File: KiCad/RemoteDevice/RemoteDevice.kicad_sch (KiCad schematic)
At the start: 55 parts, among them J1 Alim, Q1 PJA3411, Q2 PJA3411, SW1 BP, SW2 BP, U1 XC9140, U10 XBEE-3, U2 STM32L041F6Px, U3 MCP6281, U4 ADT7410TRZ, U5 MCP6281, U6 RT606, U7 Microphone, U8 LD2981CU33, U9 Con_4pts

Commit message: routage terminé, proto à envoyer à José
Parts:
- removed J1: Alim, LibKiCad_PjtDeviceManagePV:PinHeader2pts, symbol Connector:Conn_01x02_Male
- added J1, J2: pin, LibKiCad_PjtDeviceManagePV:PinHeader1Pt, symbol LibKiCad_PjtDeviceManagePV:Conn_01x01_Male
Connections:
- net GND: now also J2.1 (Pin_1)
- net piles: now also J1.1 (Pin_1)
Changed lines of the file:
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@@
+    (pin "1")
+  )
+  (symbol (lib_id "LibKiCad_PjtDeviceManagePV:Conn_01x01_Male") (at 19.05 57.15 0) (unit 1)
+    (in_bom yes) (on_board yes)
+    (property "Reference" "J2" (id 0) (at 16.51 57.15 0))
+    (property "Value" "pin" (id 1) (at 21.59 58.42 0))
+    (property "Footprint" "LibKiCad_PjtDeviceManagePV:PinHeader1Pt" (id 2) (at 19.05 57.15 0)
+      (effects (font (size 1.27 1.27)) hide)
+    )
+    (property "Datasheet" "~" (id 3) (at 19.05 57.15 0)
+      (effects (font (size 1.27 1.27)) hide)
+    )
     (pin "1")
   )
@@
     (pin "2")
     (pin "3")
-  )
-  (symbol (lib_id "Connector:Conn_01x02_Male") (at 19.05 54.61 0) (unit 1)
-    (in_bom yes) (on_board yes) (fields_autoplaced)
-    (property "Reference" "J1" (id 0) (at 19.685 49.53 0))
-    (property "Value" "Alim" (id 1) (at 19.685 52.07 0))
-    (property "Footprint" "LibKiCad_PjtDeviceManagePV:PinHeader2pts" (id 2) (at 19.05 54.61 0)
-      (effects (font (size 1.27 1.27)) hide)
-    )
-    (property "Datasheet" "~" (id 3) (at 19.05 54.61 0)
-      (effects (font (size 1.27 1.27)) hide)
-    )
-    (pin "1")
-    (pin "2")
   )
   (symbol (lib_id "power:PWR_FLAG") (at 77.47 49.53 0) (unit 1)
@@
     )
     (property "Datasheet" "" (id 3) (at 148.59 72.39 0)
+      (effects (font (size 1.27 1.27)) hide)
+    )
+    (pin "1")
+  )
+  (symbol (lib_id "LibKiCad_PjtDeviceManagePV:Conn_01x01_Male") (at 19.05 54.61 0) (unit 1)
+    (in_bom yes) (on_board yes)
+    (property "Reference" "J1" (id 0) (at 16.51 54.61 0))
+    (property "Value" "pin" (id 1) (at 21.59 52.07 0))
+    (property "Footprint" "LibKiCad_PjtDeviceManagePV:PinHeader1Pt" (id 2) (at 19.05 54.61 0)
+      (effects (font (size 1.27 1.27)) hide)
+    )
+    (property "Datasheet" "~" (id 3) (at 19.05 54.61 0)
       (effects (font (size 1.27 1.27)) hide)
     )
@@
       (reference "D4") (unit 1) (value "BAT43W-V") (footprint "Diode_SMD:D_SOD-123")
     )
-    (path "/57c017b0-5147-469f-9dad-ed678c57ce92"
-      (reference "J1") (unit 1) (value "Alim") (footprint "LibKiCad_PjtDeviceManagePV:PinHeader2pts")
+    (path "/d3ae2a9d-452c-4e1c-b009-c846d4a4e6df"
+      (reference "J1") (unit 1) (value "pin") (footprint "LibKiCad_PjtDeviceManagePV:PinHeader1Pt")
+    )
+    (path "/3c43b862-699a-4806-8267-7fe24bc43c02"
+      (reference "J2") (unit 1) (value "pin") (footprint "LibKiCad_PjtDeviceManagePV:PinHeader1Pt")
     )
     (path "/a9057e0b-279b-43fc-996f-a2889cba57e3"

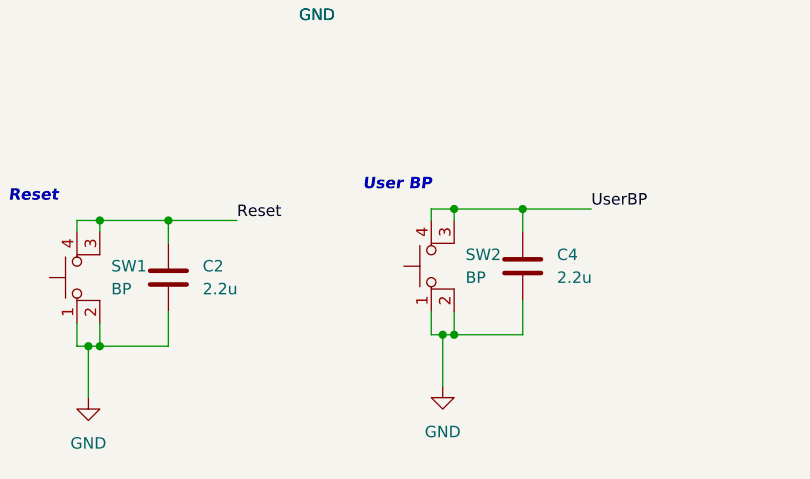
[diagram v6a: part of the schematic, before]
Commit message: Routage revu (tailles condensateur sur switchs). Version envoyée à José le 20 06 2022
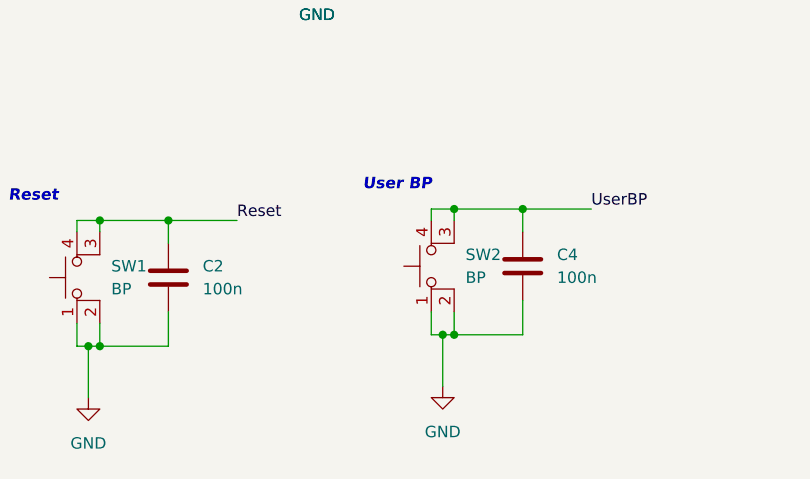
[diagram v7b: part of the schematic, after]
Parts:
- C2, C4: value 2.2u -> 100n; footprint Capacitor_SMD:C_1812_4532Metric -> Capacitor_SMD:C_1206_3216Metric
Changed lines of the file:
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@@
       (effects (font (size 1.27 1.27)) (justify left))
     )
-    (property "Value" "2.2u" (id 1) (at 77.47 172.7199 0)
-      (effects (font (size 1.27 1.27)) (justify left))
-    )
-    (property "Footprint" "Capacitor_SMD:C_1812_4532Metric" (id 2) (at 74.6252 175.26 0)
+    (property "Value" "100n" (id 1) (at 77.47 172.7199 0)
+      (effects (font (size 1.27 1.27)) (justify left))
+    )
+    (property "Footprint" "Capacitor_SMD:C_1206_3216Metric" (id 2) (at 74.6252 175.26 0)
       (effects (font (size 1.27 1.27)) hide)
     )
@@
       (effects (font (size 1.27 1.27)) (justify left))
     )
-    (property "Value" "2.2u" (id 1) (at 38.1 173.9899 0)
-      (effects (font (size 1.27 1.27)) (justify left))
-    )
-    (property "Footprint" "Capacitor_SMD:C_1812_4532Metric" (id 2) (at 35.2552 176.53 0)
+    (property "Value" "100n" (id 1) (at 38.1 173.9899 0)
+      (effects (font (size 1.27 1.27)) (justify left))
+    )
+    (property "Footprint" "Capacitor_SMD:C_1206_3216Metric" (id 2) (at 35.2552 176.53 0)
       (effects (font (size 1.27 1.27)) hide)
     )
@@
     )
     (path "/7be684da-a8e2-4205-844b-38b6f10d367e"
-      (reference "C2") (unit 1) (value "2.2u") (footprint "Capacitor_SMD:C_1812_4532Metric")
+      (reference "C2") (unit 1) (value "100n") (footprint "Capacitor_SMD:C_1206_3216Metric")
     )
     (path "/8cdfe25e-4b7d-4013-8124-b3c01f18588e"
@@
     )
     (path "/10230143-c151-439b-9c31-460a1c05ff46"
-      (reference "C4") (unit 1) (value "2.2u") (footprint "Capacitor_SMD:C_1812_4532Metric")
+      (reference "C4") (unit 1) (value "100n") (footprint "Capacitor_SMD:C_1206_3216Metric")
     )
     (path "/bf597f3e-5fb8-4897-ac09-bc00b0cf2f92"

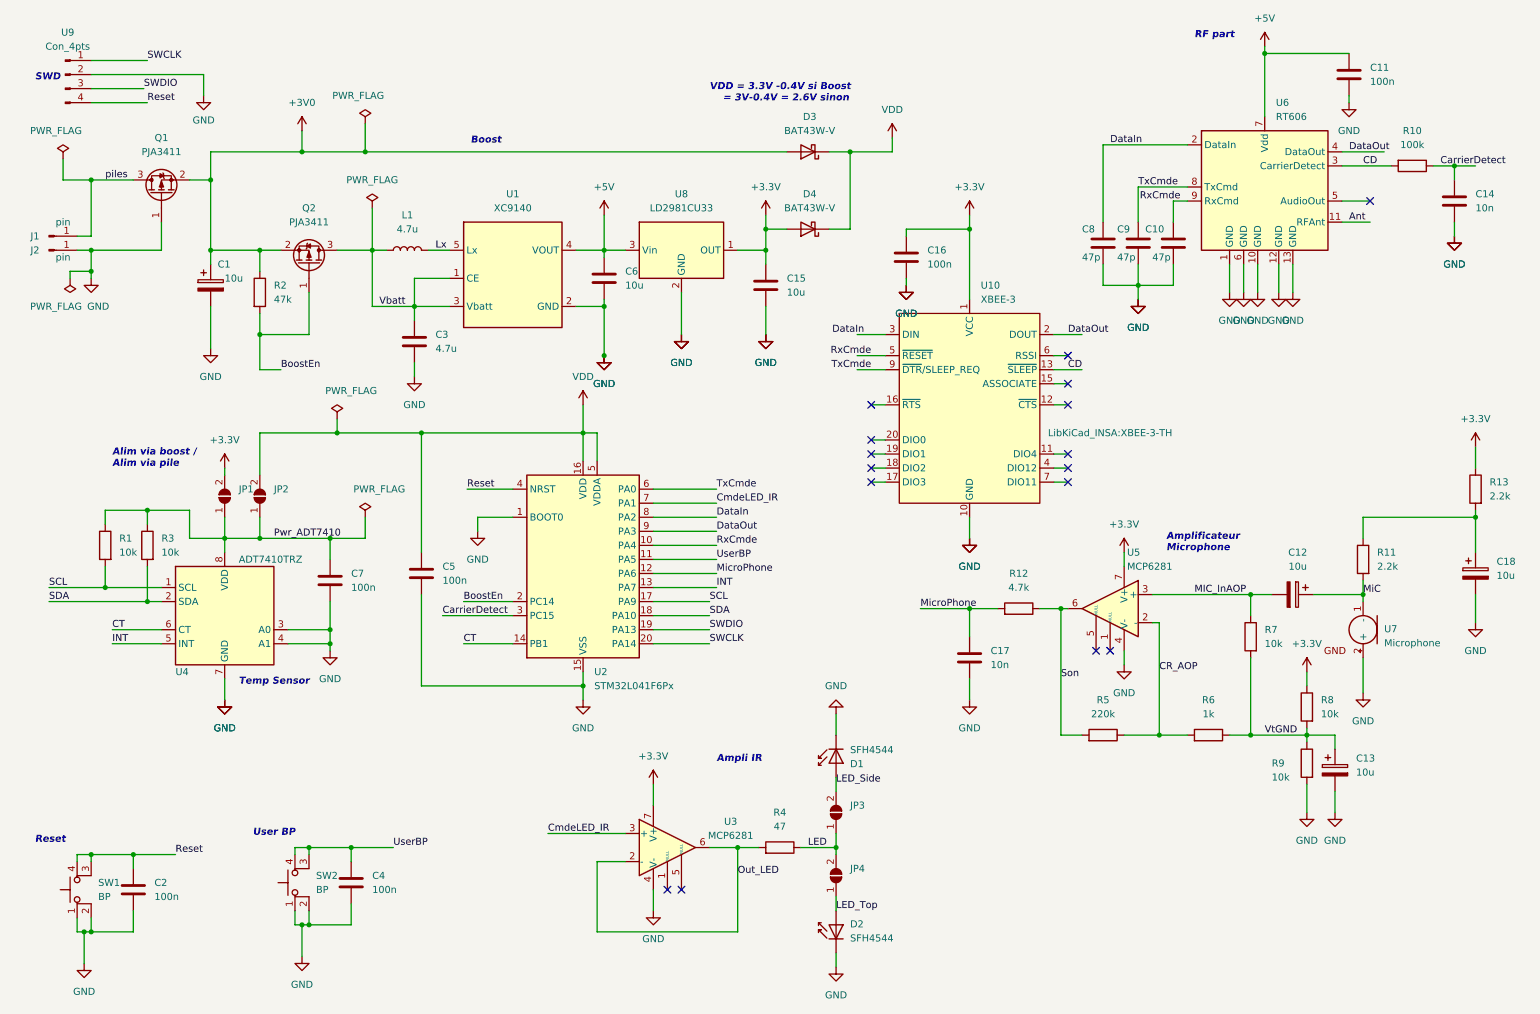
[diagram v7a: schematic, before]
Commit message: schéma revu avec quelques valeurs retouchées : val correspondent à l'assemblage. Board non mis à jour pour si peu. Le silkscreen est modifié par contre
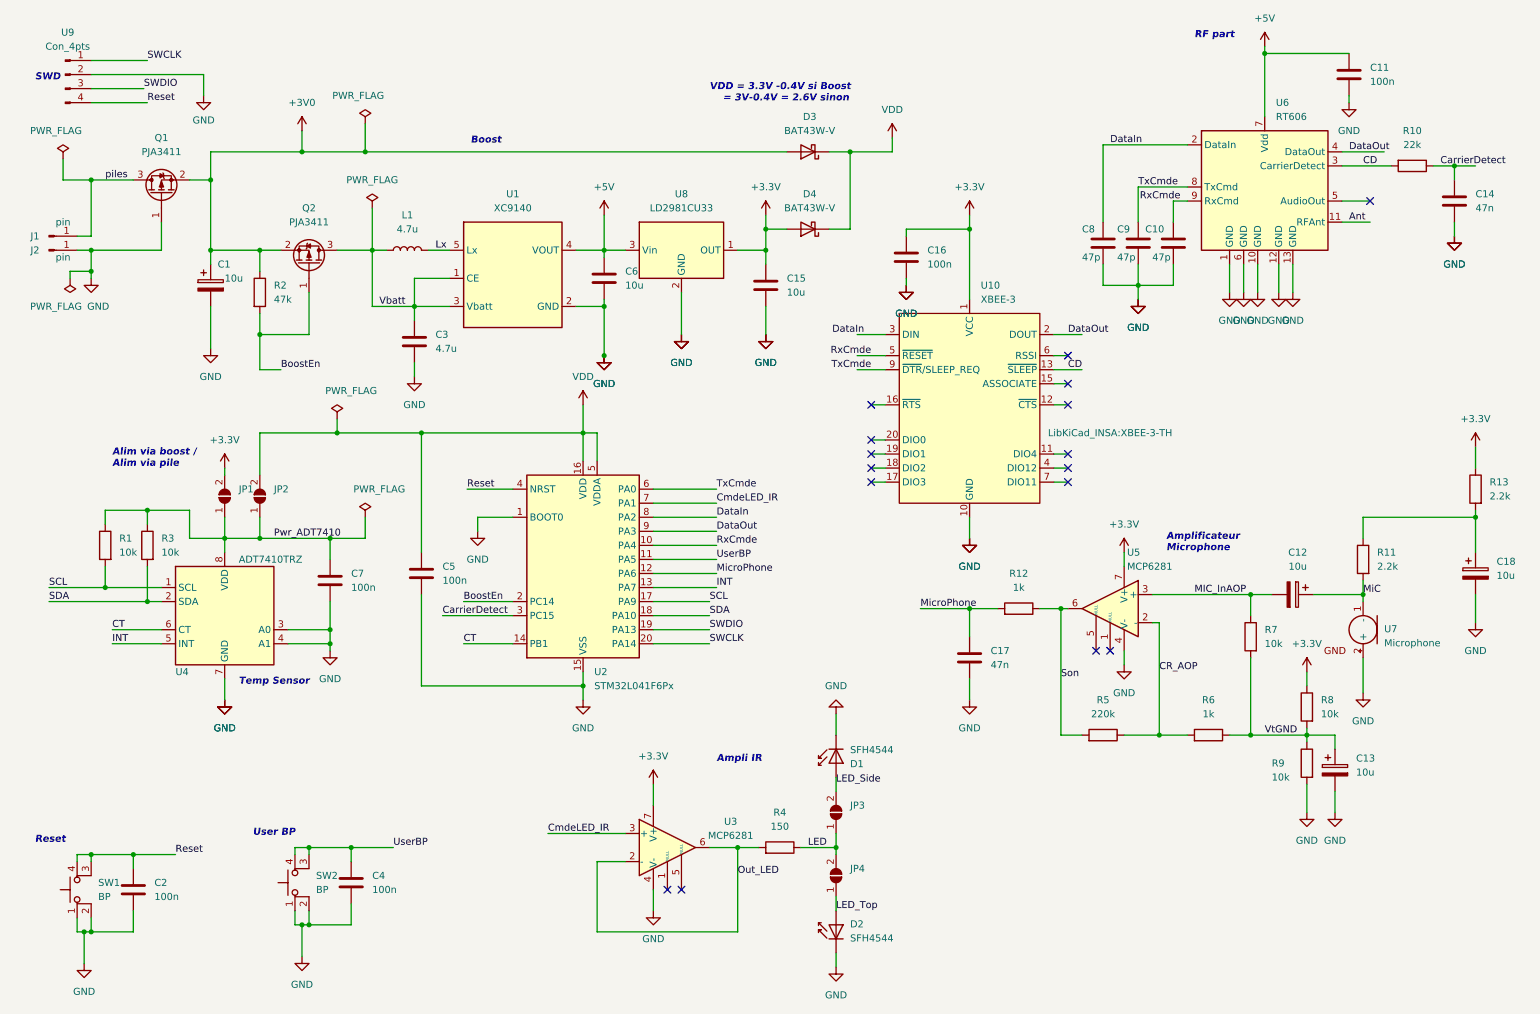
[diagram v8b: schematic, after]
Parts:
- C14, C17: value 10n -> 47n
- R10: value 100k -> 22k
- R12: value 4.7k -> 1k
- R4: value 47 -> 150
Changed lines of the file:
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@@
     (in_bom yes) (on_board yes) (fields_autoplaced)
     (property "Reference" "R4" (id 0) (at 151.13 158.75 90))
-    (property "Value" "47" (id 1) (at 151.13 161.29 90))
+    (property "Value" "150" (id 1) (at 151.13 161.29 90))
     (property "Footprint" "Resistor_SMD:R_1206_3216Metric" (id 2) (at 151.13 166.878 90)
       (effects (font (size 1.27 1.27)) hide)
@@
     (in_bom yes) (on_board yes) (fields_autoplaced)
     (property "Reference" "R12" (id 0) (at 194.31 115.57 90))
-    (property "Value" "4.7k" (id 1) (at 194.31 118.11 90))
+    (property "Value" "1k" (id 1) (at 194.31 118.11 90))
     (property "Footprint" "Resistor_SMD:R_1206_3216Metric" (id 2) (at 194.31 123.698 90)
       (effects (font (size 1.27 1.27)) hide)
@@
       (effects (font (size 1.27 1.27)) (justify left))
     )
-    (property "Value" "10n" (id 1) (at 189.23 132.0799 0)
+    (property "Value" "47n" (id 1) (at 189.23 132.0799 0)
       (effects (font (size 1.27 1.27)) (justify left))
     )
@@
     (in_bom yes) (on_board yes) (fields_autoplaced)
     (property "Reference" "R10" (id 0) (at 265.43 35.56 90))
-    (property "Value" "100k" (id 1) (at 265.43 38.1 90))
+    (property "Value" "22k" (id 1) (at 265.43 38.1 90))
     (property "Footprint" "Resistor_SMD:R_1206_3216Metric" (id 2) (at 265.43 40.132 90)
       (effects (font (size 1.27 1.27)) hide)
@@
       (effects (font (size 1.27 1.27)) (justify left))
     )
-    (property "Value" "10n" (id 1) (at 276.86 49.5299 0)
+    (property "Value" "47n" (id 1) (at 276.86 49.5299 0)
       (effects (font (size 1.27 1.27)) (justify left))
     )
@@
     )
     (path "/f2c5cc7f-598c-4c67-9e48-e6ce6b8a1303"
-      (reference "C14") (unit 1) (value "10n") (footprint "Capacitor_SMD:C_1206_3216Metric")
+      (reference "C14") (unit 1) (value "47n") (footprint "Capacitor_SMD:C_1206_3216Metric")
     )
     (path "/0a05c4db-2c3d-4165-8365-666c36e5816b"
@@
     )
     (path "/975c6117-9330-4e23-be93-b7258cda7016"
-      (reference "C17") (unit 1) (value "10n") (footprint "Capacitor_SMD:C_1206_3216Metric")
+      (reference "C17") (unit 1) (value "47n") (footprint "Capacitor_SMD:C_1206_3216Metric")
     )
     (path "/24328120-84e9-42eb-a4f4-5b935ef17915"
@@
     )
     (path "/02497bb0-4fe7-4a29-8b9d-74b1503df818"
-      (reference "R4") (unit 1) (value "47") (footprint "Resistor_SMD:R_1206_3216Metric")
+      (reference "R4") (unit 1) (value "150") (footprint "Resistor_SMD:R_1206_3216Metric")
     )
     (path "/e7c9eb43-7690-4c06-b31b-5c56ae2d664f"
@@
     )
     (path "/d46aace0-661d-49a9-9148-e3b2e1caa4bf"
-      (reference "R10") (unit 1) (value "100k") (footprint "Resistor_SMD:R_1206_3216Metric")
+      (reference "R10") (unit 1) (value "22k") (footprint "Resistor_SMD:R_1206_3216Metric")
     )
     (path "/8ad0ce48-64b5-4271-80f5-23251314bbaa"
@@
     )
     (path "/8cafa459-24f7-4ce5-bcef-ea1229a57da8"
-      (reference "R12") (unit 1) (value "4.7k") (footprint "Resistor_SMD:R_1206_3216Metric")
+      (reference "R12") (unit 1) (value "1k") (footprint "Resistor_SMD:R_1206_3216Metric")
     )
     (path "/1fa3e610-db57-449d-8acc-dccd514b7896"
